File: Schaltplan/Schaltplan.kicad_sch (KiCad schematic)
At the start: 20 parts, among them J1 Conn_01x02_Pin, J2 Conn_01x02_Pin, J3 LM2577 DC-DC Step-Up Modul, Q1 IRLZ44N, Q2 IRLZ44N, U1 ACS712xLCTR-05B

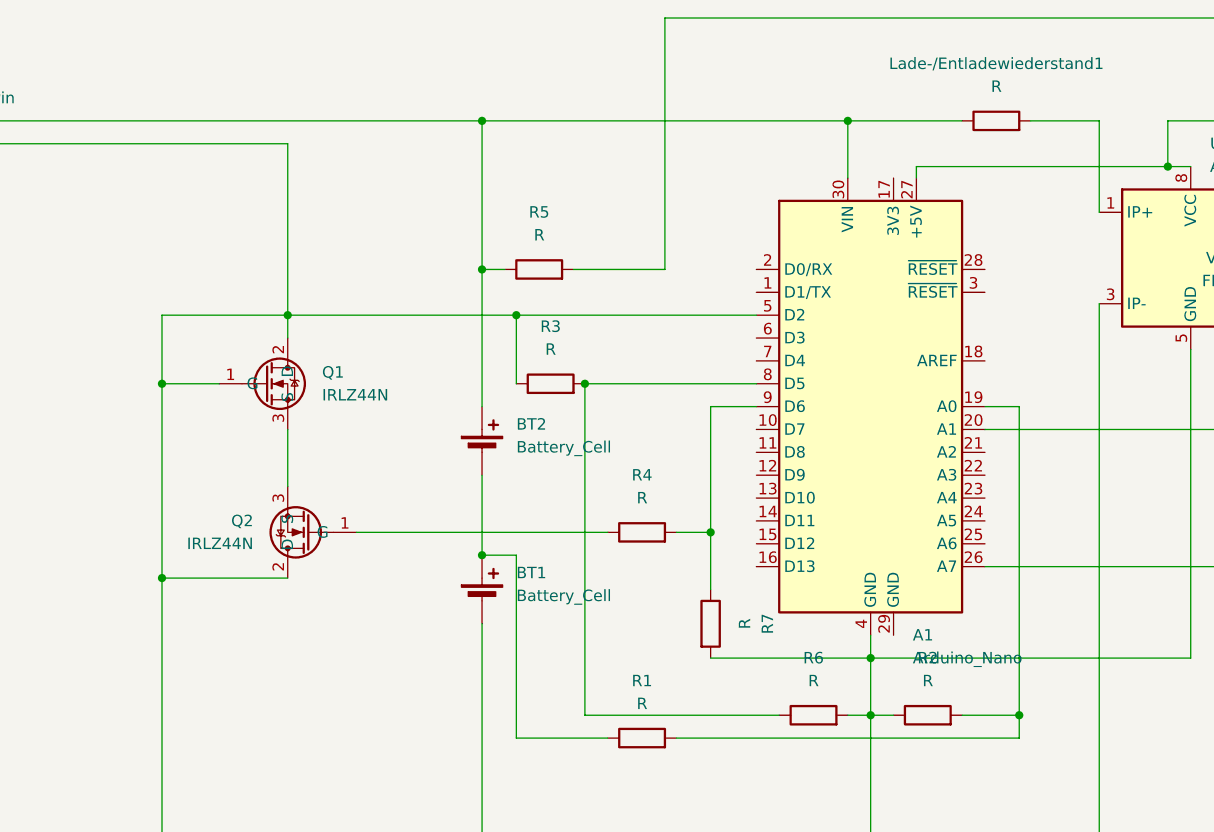
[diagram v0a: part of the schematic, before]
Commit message: Refactor schematic by removing unused junctions and wires for improved clarity
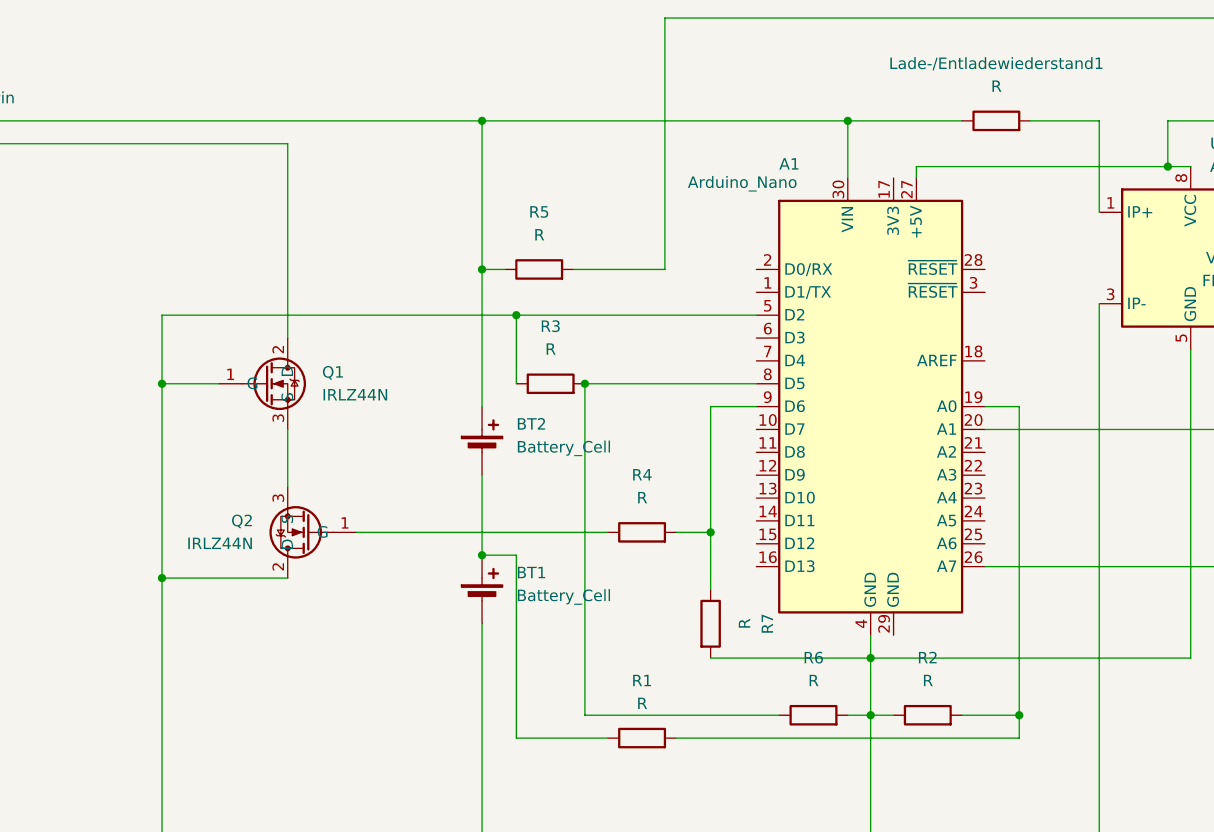
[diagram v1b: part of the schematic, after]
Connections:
- net at A1.4 (GND), A1.5 (D2), BT1.2 (-)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: no longer J1.2 (Pin_2), Q1.2 (D)
- new net: J1.2 (Pin_2), Q1.2 (D)
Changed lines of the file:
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@@
-	)
-	(junction
-		(at 104.14 76.2)
-		(diameter 0)
-		(color 0 0 0 0)
 	)
 	(junction
@@
 	(wire
 		(pts
-			(xy 104.14 76.2) (xy 104.14 57.15)
-		)
-		(stroke
-			(width 0)
-			(type default)
-		)
-	)
-	(wire
-		(pts
 			(xy 194.31 54.61) (xy 194.31 64.77)
 		)
@@
 	(wire
 		(pts
-			(xy 104.14 78.74) (xy 104.14 76.2)
+			(xy 104.14 57.15) (xy 104.14 78.74)
 		)
 		(stroke
@@
 	(wire
 		(pts
-			(xy 104.14 76.2) (xy 129.54 76.2)
-		)
-		(stroke
-			(width 0)
-			(type default)
-		)
-	)
-	(wire
-		(pts
 			(xy 125.73 102.87) (xy 125.73 93.98)
 		)
@@
 	(wire
 		(pts
-			(xy 104.14 76.2) (xy 90.17 76.2)
+			(xy 90.17 76.2) (xy 129.54 76.2)
 		)
 		(stroke
@@
 		(on_board yes)
 		(dnp no)
-		(fields_autoplaced yes)
 		(property "Reference" "A1"
-			(at 173.5933 111.76 0)
+			(at 158.75 59.436 0)
 			(effects
 				(font
@@
 		)
 		(property "Value" "Arduino_Nano"
-			(at 173.5933 114.3 0)
-			(effects
-				(font
+			(at 148.59 61.468 0)
+			(effects
+				(font

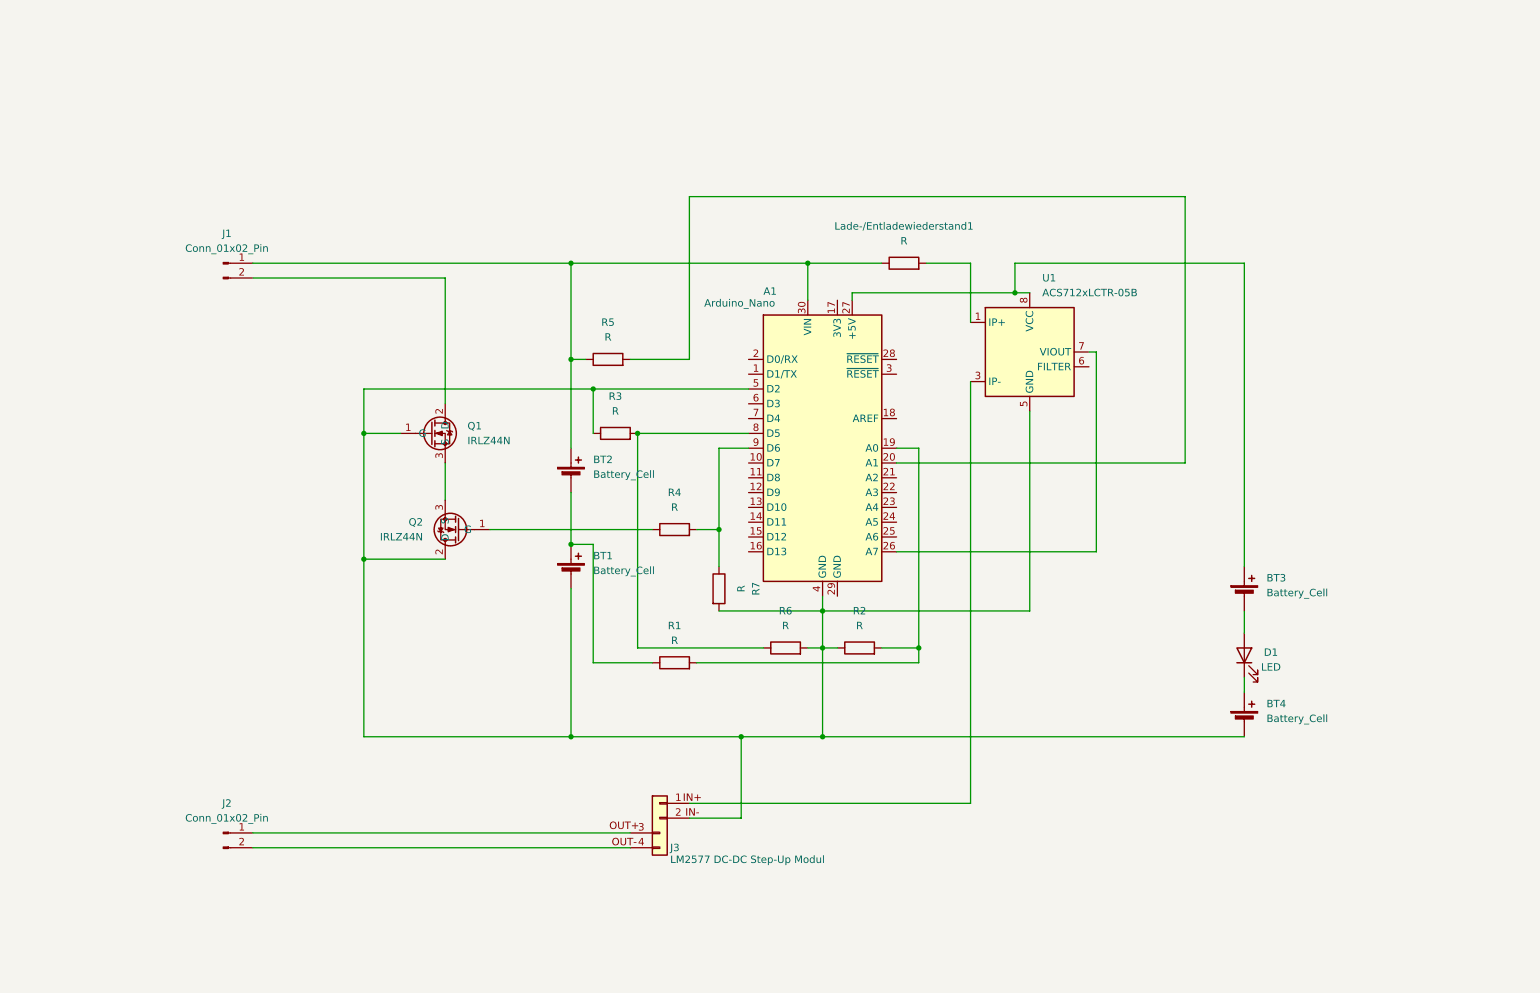
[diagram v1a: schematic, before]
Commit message: Complete Schaltplan remake
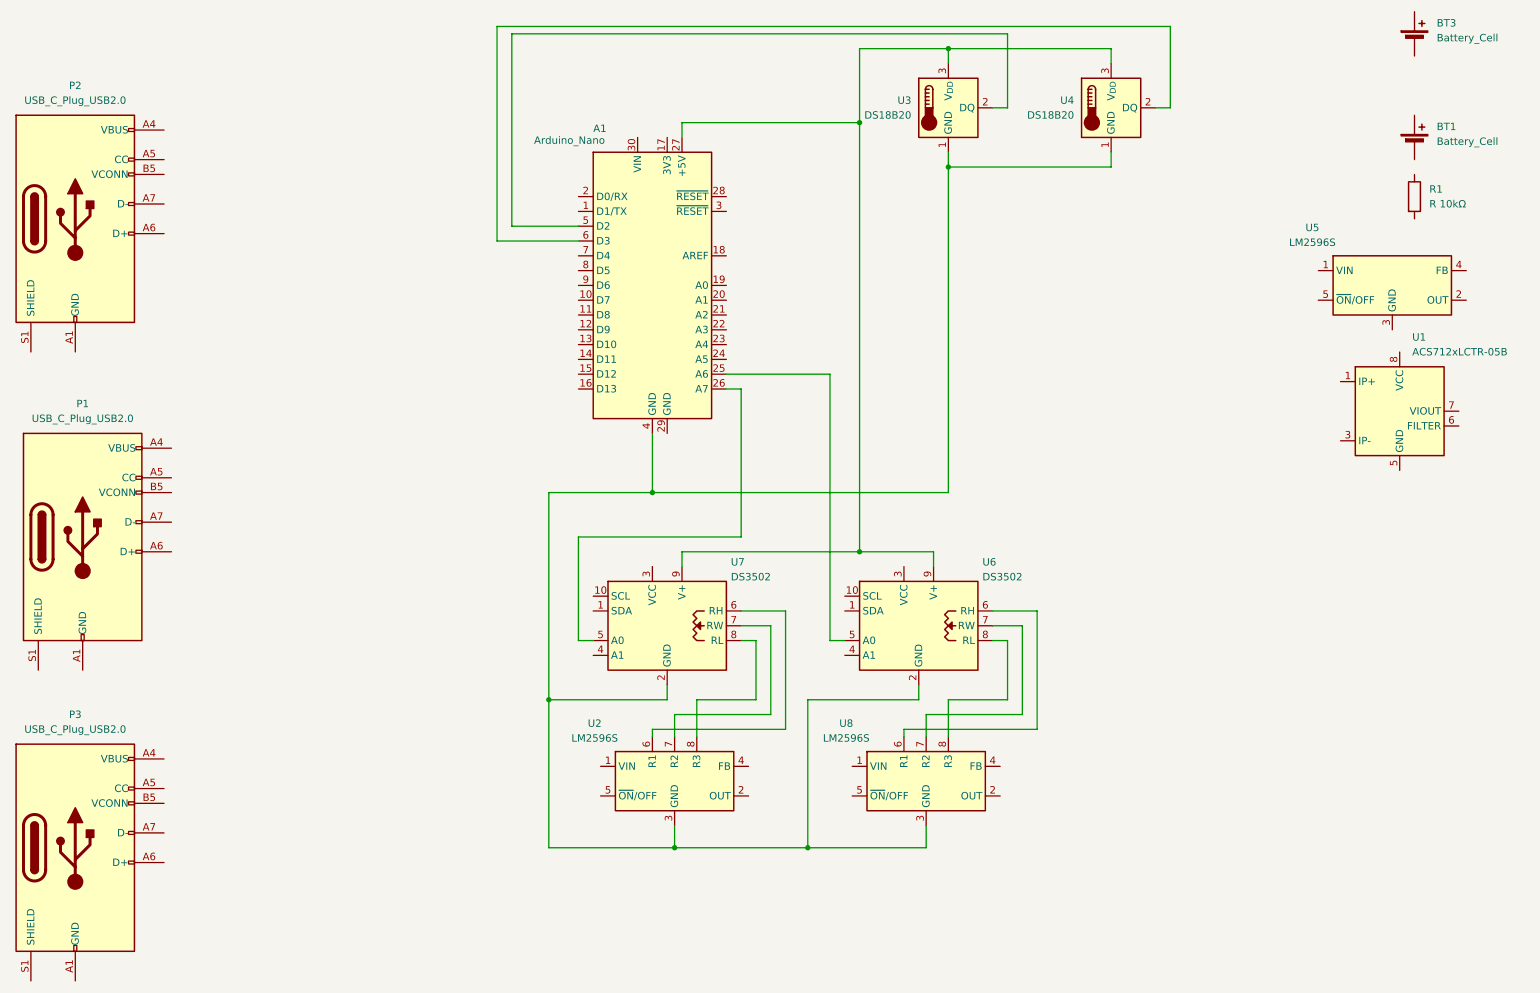
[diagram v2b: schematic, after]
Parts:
- removed BT2, BT4: Battery_Cell, symbol Device:Battery_Cell
- removed D1: LED, symbol Device:LED
- removed J1, J2: Conn_01x02_Pin, symbol Connector:Conn_01x02_Pin
- removed J3: LM2577 DC-DC Step-Up Modul, symbol Connector_Generic:Conn_01x04
- removed Lade-/Entladewiederstand1, R2, R3, R4, R5, R6, R7: R, symbol Device:R
- removed Q1, Q2: IRLZ44N, Package_TO_SOT_THT:TO-220-3_Vertical, symbol Transistor_FET:IRLZ44N
- added P1, P2, P3: USB_C_Plug_USB2.0, symbol Connector:USB_C_Plug_USB2.0
- added U2, U5, U8: LM2596S, Package_TO_SOT_SMD:TO-263-5_TabPin3, symbol Regulator_Switching:LM2596S-5
- added U3, U4: DS18B20, Package_TO_SOT_THT:TO-92_Inline, symbol Sensor_Temperature:DS18B20
- added U6, U7: DS3502, Package_SO:MSOP-10_3x3mm_P0.5mm, symbol Potentiometer_Digital:DS3502
- R1: value R -> R 10kΩ
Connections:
- net at BT1.1 (+): no longer R1.1
- net at R1.2: no longer A1.19 (A0)
- net at U1.7 (VIOUT): no longer A1.26 (A7)
- net at A1.25 (A6): now also U6.5 (A0)
- net at A1.6 (D3): now also U4.2 (DQ)
- new net: A1.4 (GND), U2.3 (GND), U3.1 (GND), U4.1 (GND), U6.2 (GND), U7.2 (GND), U8.3 (GND)
- new net: U6.6 (RH), U8.6 (R1)
- new net: U6.7 (RW), U8.7 (R2)
- new net: U6.8 (RL), U8.8 (R3)
- new net: P3.A1 (GND), P3.A12 (GND), P3.B1 (GND), P3.B12 (GND)
- new net: P3.A4 (VBUS), P3.A9 (VBUS), P3.B4 (VBUS), P3.B9 (VBUS)
- new net: A1.5 (D2), U3.2 (DQ)
- new net: A1.27 (+5V), U3.3 (V_{DD}), U4.3 (V_{DD}), U6.9 (V+), U7.9 (V+)
- new net: U2.6 (R1), U7.6 (RH)
- new net: U2.7 (R2), U7.7 (RW)
- new net: U2.8 (R3), U7.8 (RL)
- new net: A1.26 (A7), U7.5 (A0)
- new net: P1.A1 (GND), P1.A12 (GND), P1.B1 (GND), P1.B12 (GND)
- new net: P1.A4 (VBUS), P1.A9 (VBUS), P1.B4 (VBUS), P1.B9 (VBUS)
- new net: P2.A1 (GND), P2.A12 (GND), P2.B1 (GND), P2.B12 (GND)
- new net: P2.A4 (VBUS), P2.A9 (VBUS), P2.B4 (VBUS), P2.B9 (VBUS)
- now unconnected: BT1.2 (-), BT3.1 (+), U1.5 (GND), U1.8 (VCC)
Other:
- moved on the sheet: A1
